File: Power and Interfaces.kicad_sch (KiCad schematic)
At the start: 33 parts, among them J5 Molex 43650-0500, J6 Molex 43650-0500, U3 TPS54302, U5 TLV74033PDBVR

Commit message: updated pinout, begin layout
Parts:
- renumbered C25 to C10, C24 to C11, C4 to C12, C21 to C13, C22 to C14, C28 to C15, C27 to C16, C29 to C17, C19 to C9, D2 to D4, D7 to D5, D13 to D6, D14 to D7, D15 to D8, D5 to D9, J5 to J3, J6 to J4, R9 to R12, R10 to R13, R7 to R14, R8 to R15, R13 to R16, R14 to R17, R22 to R18, R23 to R19, R24 to R20, U3 to U2, U5 to U3
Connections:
- net +12V: now also C10.1, C11.1, D5.1 (K), U2.3 (VIN); no longer D5.2 (A), F1.2
- new net: D5.2 (A), F1.2
- no-connect marks 0 -> 1
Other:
- moved on the sheet: C9, D4, D5, R12, R13

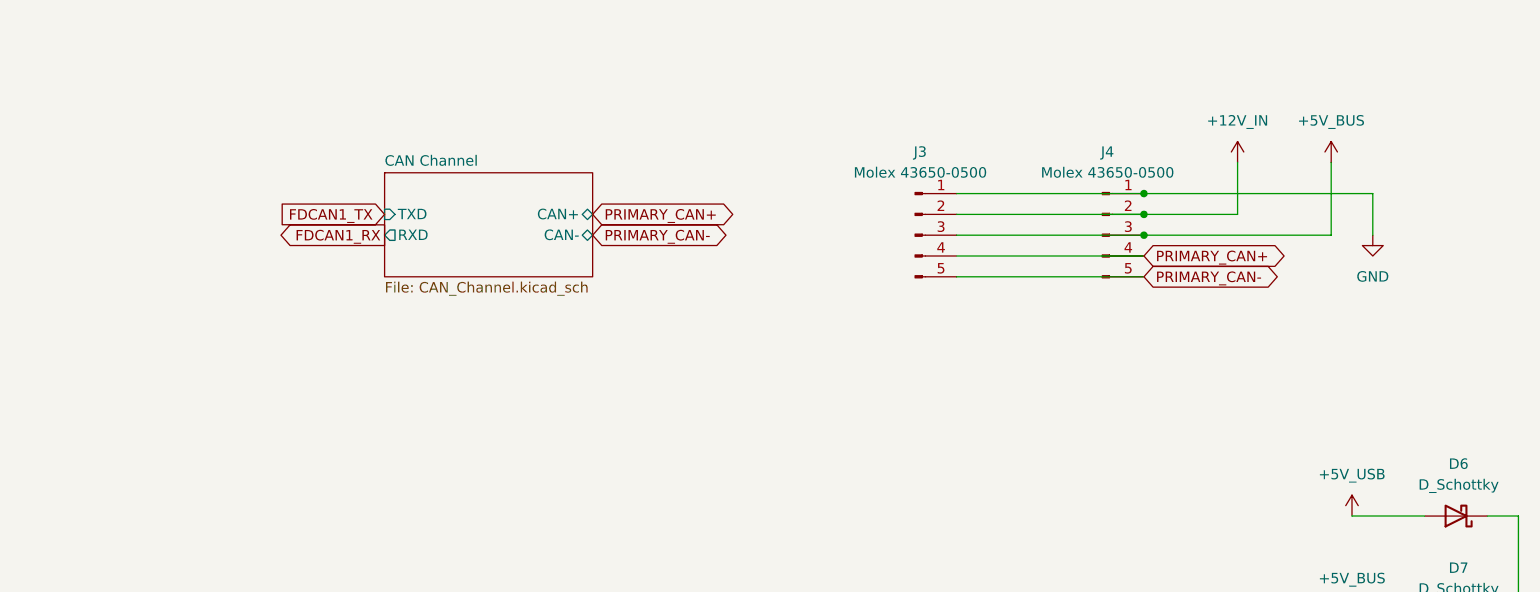
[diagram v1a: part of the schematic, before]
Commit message: add second CAN and backup domain components
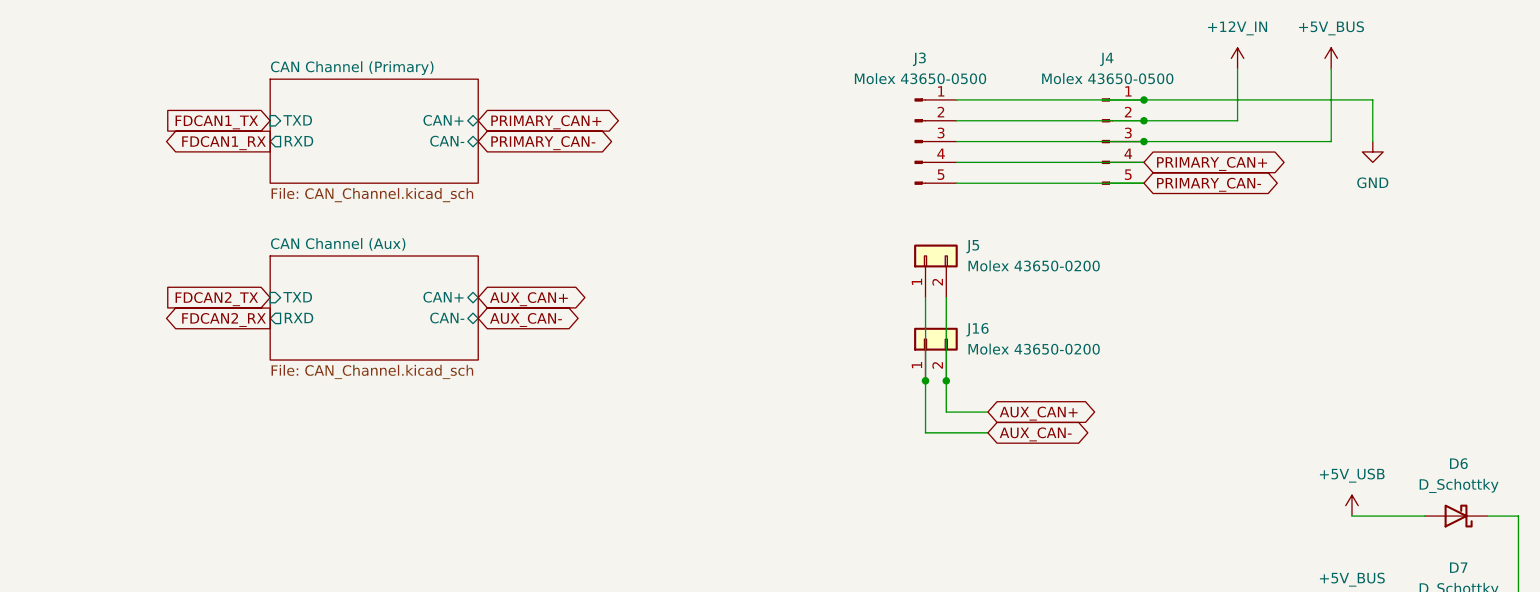
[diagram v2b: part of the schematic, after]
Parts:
- added J16, J5: Molex 43650-0200, Connector_Molex:Molex_Micro-Fit_3.0_43650-0200_1x02_P3.00mm_Horizontal, symbol Connector_Generic:Conn_01x02
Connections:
- new net AUX_CAN+: J16.2 (Pin_2), J5.2 (Pin_2)
- new net AUX_CAN-: J16.1 (Pin_1), J5.1 (Pin_1)
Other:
- sheet CAN Channel renamed CAN Channel (Primary)
- added sheet CAN Channel (Aux) (CAN_Channel.kicad_sch)
- moved on the sheet: J3, J4

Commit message: dual H/V compatible Molex footprints, corrected STM32 pinout
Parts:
- J16, J5: footprint Connector_Molex:Molex_Micro-Fit_3.0_43650-0200_1x02_P3.00mm_Horizontal -> Project_Library:Molex_Micro-Fit_3.0_43650-0200_1x02_P3.00mm_Horizontal_VerticalCompatible
- J3, J4: footprint Connector_Molex:Molex_Micro-Fit_3.0_43650-0500_1x05_P3.00mm_Horizontal -> Project_Library:Molex_Micro-Fit_3.0_43650-0500_1x05_P3.00mm_Horizontal_VerticalCompatible
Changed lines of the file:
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@@
 			)
 		)
-		(property "Footprint" "Connector_Molex:Molex_Micro-Fit_3.0_43650-0500_1x05_P3.00mm_Horizontal"
+		(property "Footprint" "Project_Library:Molex_Micro-Fit_3.0_43650-0500_1x05_P3.00mm_Horizontal_VerticalCompatible"
 			(at 158.75 46.99 0)
 			(hide yes)
@@
 			)
 		)
-		(property "Footprint" "Connector_Molex:Molex_Micro-Fit_3.0_43650-0200_1x02_P3.00mm_Horizontal"
+		(property "Footprint" "Project_Library:Molex_Micro-Fit_3.0_43650-0200_1x02_P3.00mm_Horizontal_VerticalCompatible"
 			(at 137.16 71.12 0)
 			(hide yes)
@@
 			)
 		)
-		(property "Footprint" "Connector_Molex:Molex_Micro-Fit_3.0_43650-0500_1x05_P3.00mm_Horizontal"
+		(property "Footprint" "Project_Library:Molex_Micro-Fit_3.0_43650-0500_1x05_P3.00mm_Horizontal_VerticalCompatible"
 			(at 135.89 46.99 0)
 			(hide yes)
@@
 			)
 		)
-		(property "Footprint" "Connector_Molex:Molex_Micro-Fit_3.0_43650-0200_1x02_P3.00mm_Horizontal"
+		(property "Footprint" "Project_Library:Molex_Micro-Fit_3.0_43650-0200_1x02_P3.00mm_Horizontal_VerticalCompatible"
 			(at 137.16 60.96 0)
 			(hide yes)

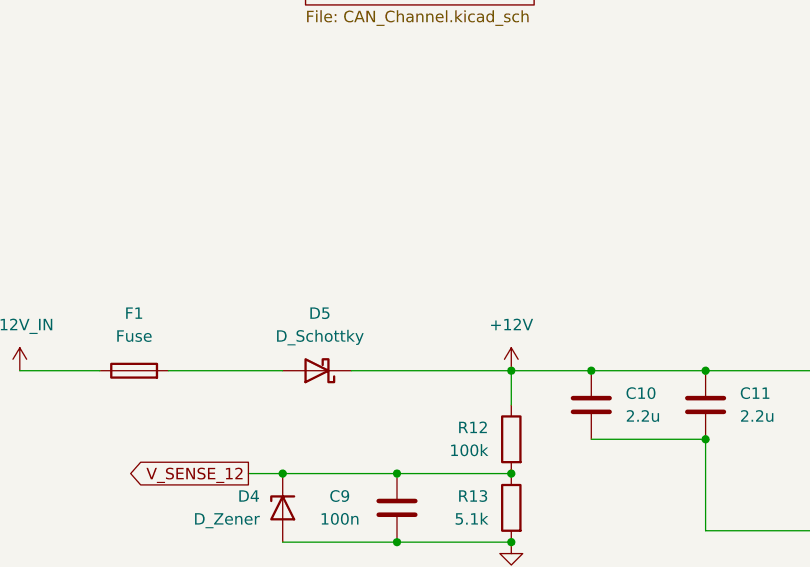
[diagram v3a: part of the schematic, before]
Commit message: add electrolytic capacitors and minor layout and silkscreen adjustments
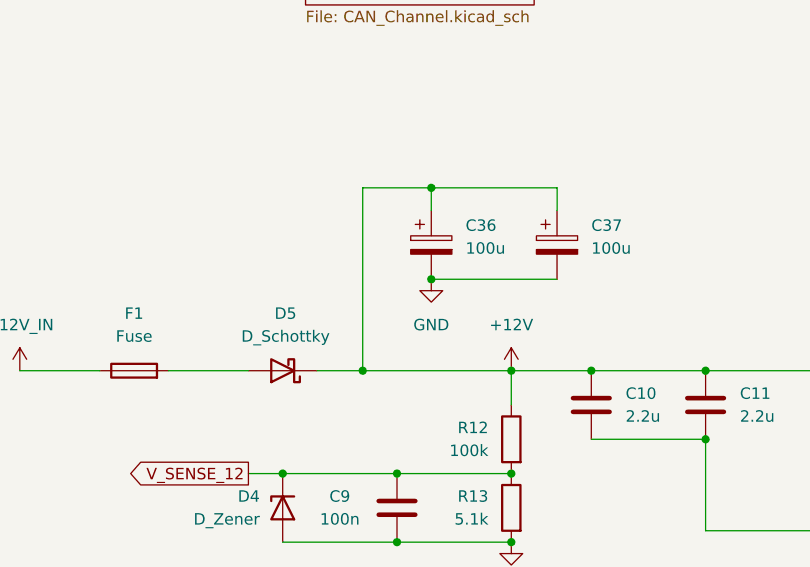
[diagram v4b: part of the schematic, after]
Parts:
- added C36, C37: 100u, Capacitor_THT:CP_Radial_D6.3mm_P2.50mm, symbol Device:C_Polarized
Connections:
- net +12V: now also C36.1, C37.1
- net GND: now also C36.2, C37.2
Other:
- moved on the sheet: D5

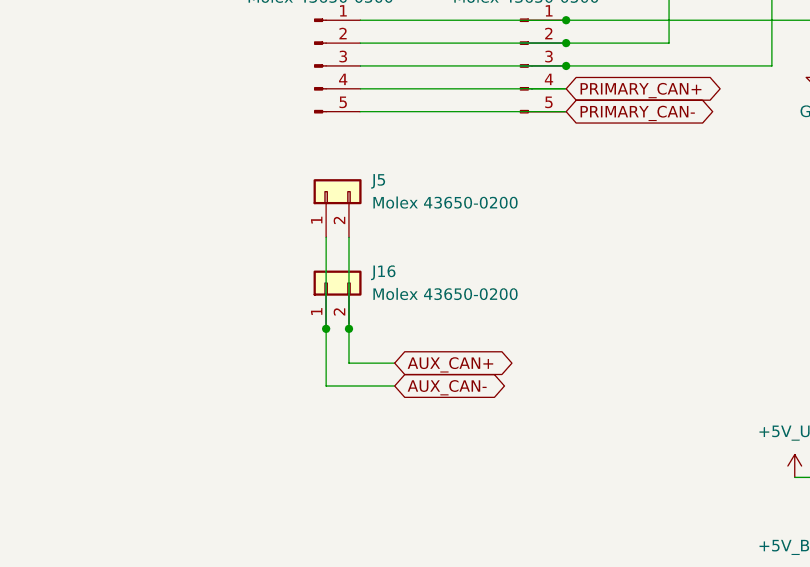
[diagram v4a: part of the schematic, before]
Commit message: copy from SwitchSense, update schematic, begin redoing layout
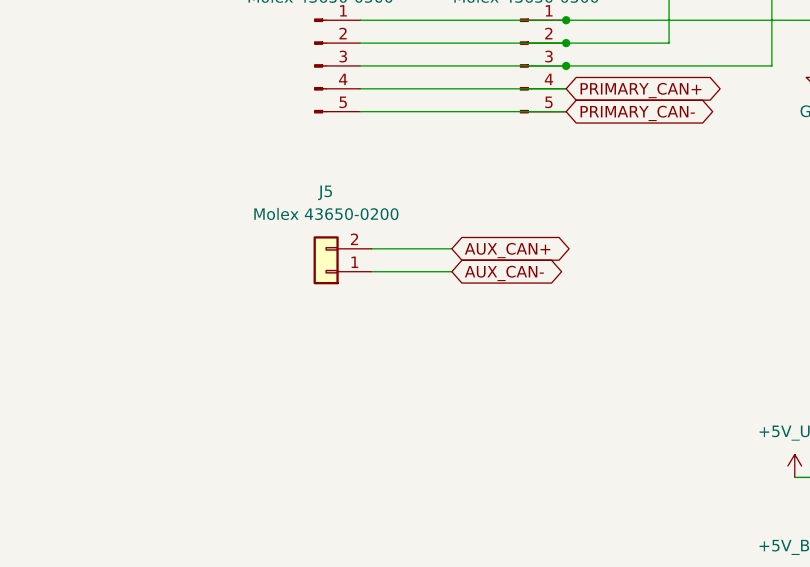
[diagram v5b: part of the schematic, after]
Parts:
- removed J16: Molex 43650-0200, Project_Library:Molex_Micro-Fit_3.0_43650-0200_1x02_P3.00mm_Horizontal_VerticalCompatible, symbol Connector_Generic:Conn_01x02
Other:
- moved on the sheet: J5

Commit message: initial layout
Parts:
- J3, J4: footprint Project_Library:Molex_Micro-Fit_3.0_43650-0500_1x05_P3.00mm_Horizontal_VerticalCompatible -> Connector_Molex:Molex_Micro-Fit_3.0_43650-0515_1x05_P3.00mm_Vertical
- J5: footprint Project_Library:Molex_Micro-Fit_3.0_43650-0200_1x02_P3.00mm_Horizontal_VerticalCompatible -> Connector_Molex:Molex_Micro-Fit_3.0_43650-0215_1x02_P3.00mm_Vertical
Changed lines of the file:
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@@
 			)
 		)
-		(property "Footprint" "Project_Library:Molex_Micro-Fit_3.0_43650-0500_1x05_P3.00mm_Horizontal_VerticalCompatible"
+		(property "Footprint" "Connector_Molex:Molex_Micro-Fit_3.0_43650-0515_1x05_P3.00mm_Vertical"
 			(at 158.75 46.99 0)
 			(hide yes)
@@
 			)
 		)
-		(property "Footprint" "Project_Library:Molex_Micro-Fit_3.0_43650-0500_1x05_P3.00mm_Horizontal_VerticalCompatible"
+		(property "Footprint" "Connector_Molex:Molex_Micro-Fit_3.0_43650-0515_1x05_P3.00mm_Vertical"
 			(at 135.89 46.99 0)
 			(hide yes)
@@
 			)
 		)
-		(property "Footprint" "Project_Library:Molex_Micro-Fit_3.0_43650-0200_1x02_P3.00mm_Horizontal_VerticalCompatible"
+		(property "Footprint" "Connector_Molex:Molex_Micro-Fit_3.0_43650-0215_1x02_P3.00mm_Vertical"
 			(at 137.16 69.85 0)
 			(hide yes)

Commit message: r0 final
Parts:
- removed D4, D9: D_Zener, Diode_SMD:D_SOD-323_HandSoldering, symbol Device:D_Zener
- renumbered C9 to C13, C36 to C14, C37 to C15, C10 to C16, C11 to C17, C12 to C18, C13 to C19, C14 to C20, C15 to C21, C16 to C22, C17 to C23, D7 to D10, D8 to D11, D10 to D12, D11 to D13, D12 to D14, D5 to D8, D6 to D9, J3 to J10, J5 to J11, J4 to J12, R12 to R22, R13 to R23, R14 to R24, R15 to R25, R16 to R26, R17 to R27, R18 to R28, R19 to R29, R20 to R30
